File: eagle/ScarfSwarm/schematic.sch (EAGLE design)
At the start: 8 parts, among them IC1 WS2811-SOP8, M1 WIRELESS-NRF24L01

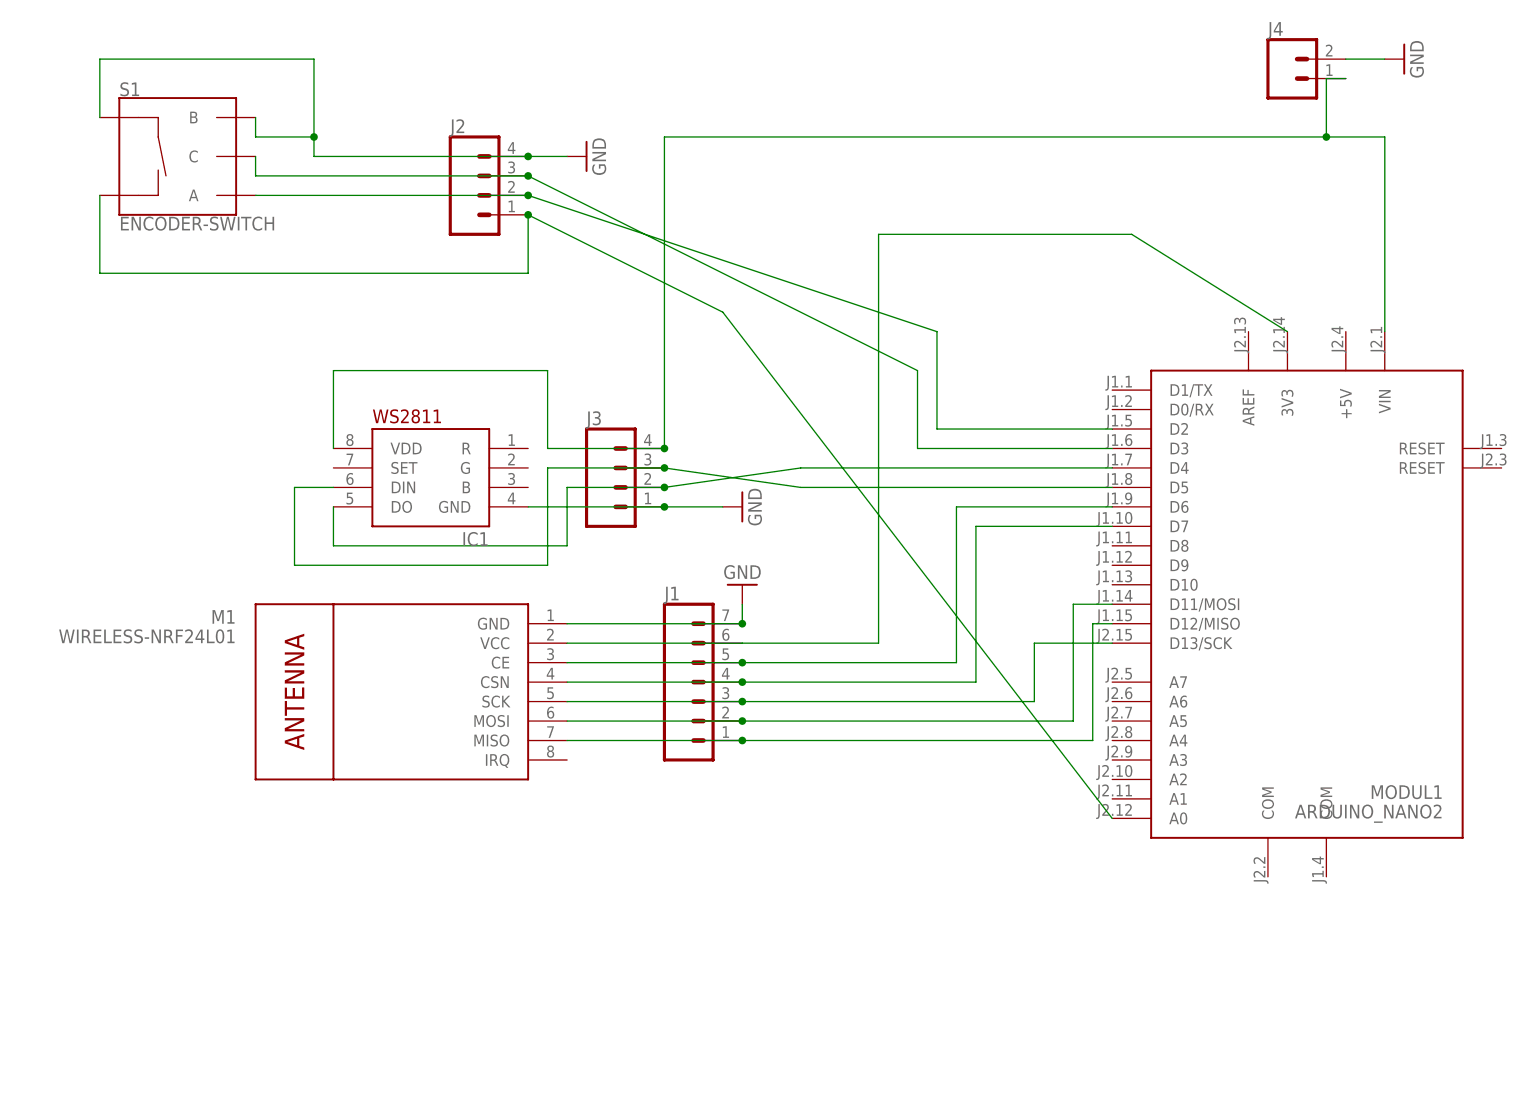
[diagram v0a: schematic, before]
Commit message: try trimming off th external componetns, first board layout
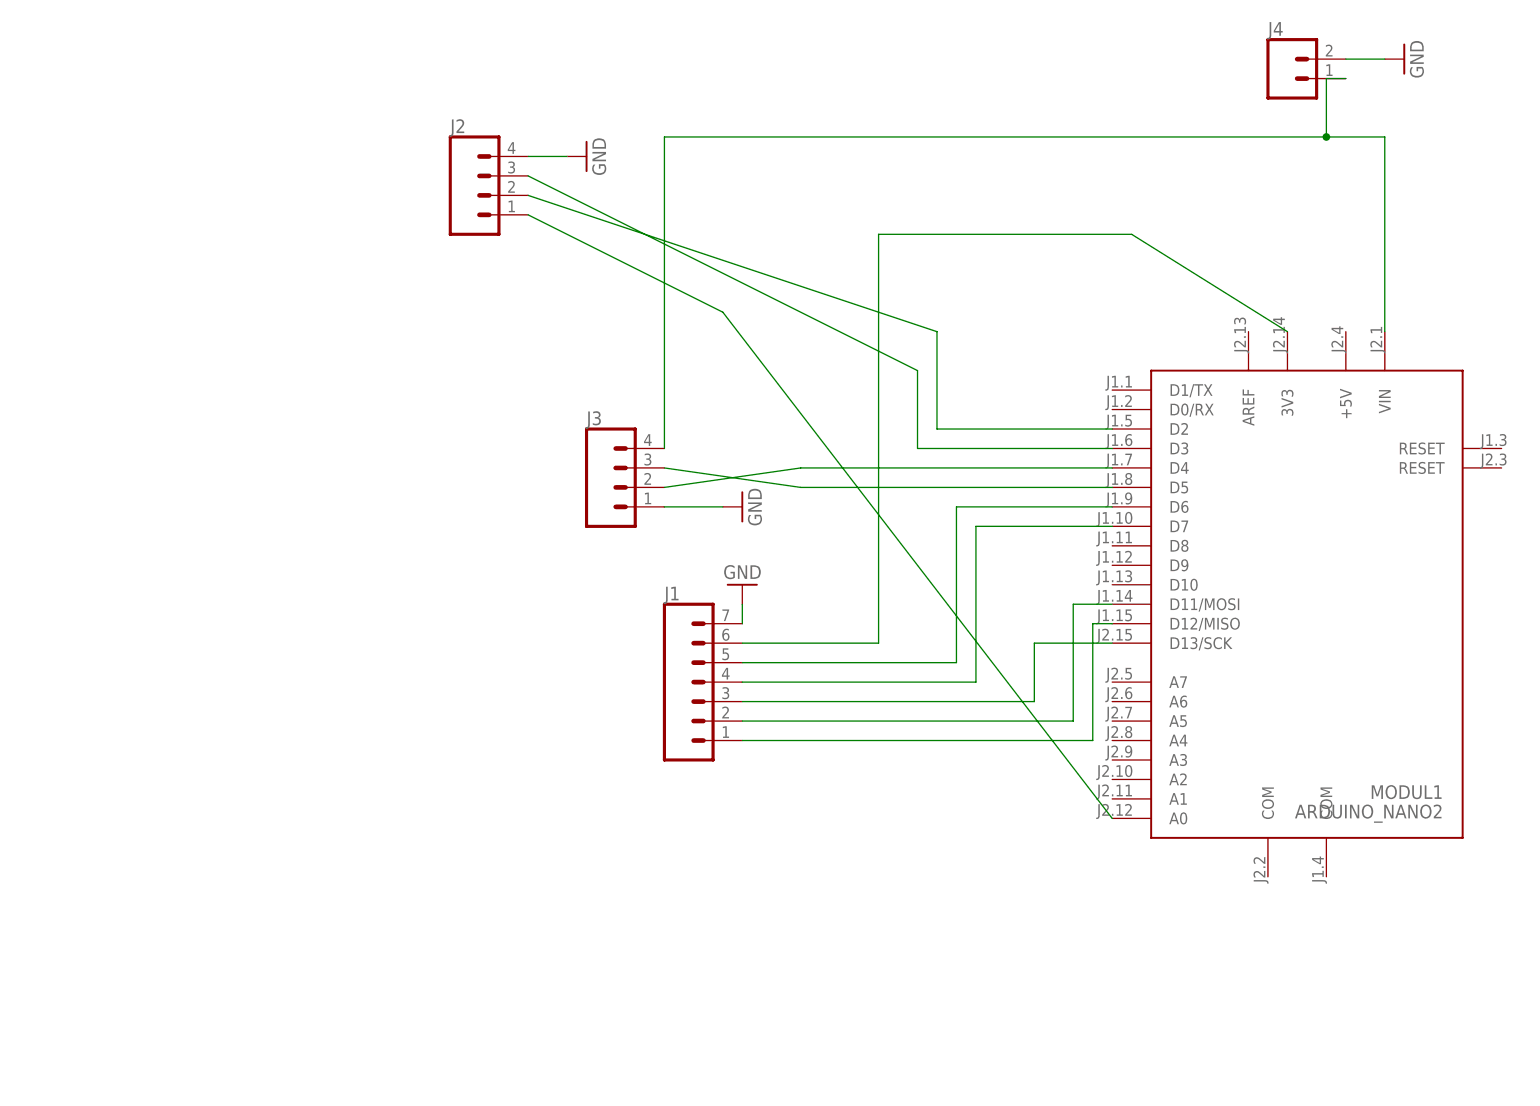
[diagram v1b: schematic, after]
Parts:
- removed IC1: WS2811-SOP8, adafruit:WS2811-SOP8
- removed M1: WIRELESS-NRF24L01, diy-modules (1):WIRELESS-NRF24L01
- removed S1: ENCODER-SWITCH, SparkFun-Switches:ENCODER-SWITCH
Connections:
- removed net N$7: IC1.DIN, J3.3, MODUL1.D5
- new net N$13: J3.3, MODUL1.D5
- net GND: no longer IC1.GND, M1.GND, S1.B, S1.SW+
- net N$1: no longer M1.VCC
- net N$10: no longer S1.A
- net N$11: no longer S1.SW-
- net N$12: no longer IC1.VDD
- net N$2: no longer M1.CE
- net N$3: no longer M1.CSN
- net N$4: no longer M1.SCK
- net N$5: no longer M1.MOSI
- net N$6: no longer M1.MISO
- net N$8: no longer IC1.DO
- net N$9: no longer S1.C
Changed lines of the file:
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@@
 <parts>
 <part name="MODUL1" library="arduino" deviceset="ARDUINO_NANO2" device=""/>
-<part name="S1" library="SparkFun-Switches" deviceset="ENCODER-SWITCH" device=""/>
 <part name="GND1" library="supply1" library_urn="urn:adsk.eagle:library:371" deviceset="GND" device=""/>
-<part name="IC1" library="adafruit" deviceset="WS2811" device="-SOP8"/>
-<part name="M1" library="diy-modules (1)" deviceset="WIRELESS-NRF24L01" device=""/>
 <part name="GND3" library="supply1" library_urn="urn:adsk.eagle:library:371" deviceset="GND" device=""/>
 <part name="GND4" library="supply1" library_urn="urn:adsk.eagle:library:371" deviceset="GND" device=""/>
@@
 <attribute name="VALUE" x="132.08" y="0" size="1.778" layer="96" rot="MR0"/>
 </instance>
-<instance part="S1" gate="G$1" x="-33.02" y="86.36" smashed="yes">
-<attribute name="NAME" x="-40.64" y="94.234" size="1.778" layer="95" font="vector"/>
-<attribute name="VALUE" x="-40.64" y="78.486" size="1.778" layer="96" font="vector" align="top-left"/>
-</instance>
 <instance part="GND1" gate="1" x="20.32" y="86.36" smashed="yes" rot="R90">
 <attribute name="VALUE" x="22.86" y="83.82" size="1.778" layer="96" rot="R90"/>
-</instance>
-<instance part="IC1" gate="G$1" x="0" y="43.18" smashed="yes" rot="MR0">
-<attribute name="NAME" x="7.62" y="35.56" size="1.778" layer="95" rot="MR0"/>
-</instance>
-<instance part="M1" gate="G$1" x="-5.08" y="15.24" smashed="yes" rot="MR0">
-<attribute name="NAME" x="-25.4" y="25.4" size="1.778" layer="95" rot="MR0"/>
-<attribute name="VALUE" x="-25.4" y="22.86" size="1.778" layer="96" rot="MR0"/>
 </instance>
 <instance part="GND3" gate="1" x="40.64" y="40.64" smashed="yes" rot="R90">
@@
 <pinref part="GND4" gate="1" pin="GND"/>
 <wire x1="40.64" y1="25.4" x2="40.64" y2="27.94" width="0.1524" layer="91"/>
-<pinref part="M1" gate="G$1" pin="GND"/>
-<wire x1="40.64" y1="25.4" x2="17.78" y2="25.4" width="0.1524" layer="91"/>
-<junction x="40.64" y="25.4"/>
 </segment>
 <segment>
-<pinref part="IC1" gate="G$1" pin="GND"/>
 <pinref part="J3" gate="J1" pin="1"/>
-<wire x1="12.7" y1="40.64" x2="30.48" y2="40.64" width="0.1524" layer="91"/>
 <pinref part="GND3" gate="1" pin="GND"/>
 <wire x1="30.48" y1="40.64" x2="38.1" y2="40.64" width="0.1524" layer="91"/>
-<junction x="30.48" y="40.64"/>
 </segment>
 <segment>
@@
 <pinref part="GND1" gate="1" pin="GND"/>
 <wire x1="12.7" y1="86.36" x2="17.78" y2="86.36" width="0.1524" layer="91"/>
-<pinref part="S1" gate="G$1" pin="SW+"/>
-<wire x1="-43.18" y1="91.44" x2="-43.18" y2="99.06" width="0.1524" layer="91"/>
-<wire x1="-43.18" y1="99.06" x2="-15.24" y2="99.06" width="0.1524" layer="91"/>
-<wire x1="-15.24" y1="99.06" x2="-15.24" y2="88.9" width="0.1524" layer="91"/>
-<wire x1="-15.24" y1="88.9" x2="-15.24" y2="86.36" width="0.1524" layer="91"/>
-<wire x1="-15.24" y1="86.36" x2="12.7" y2="86.36" width="0.1524" layer="91"/>
-<junction x="12.7" y="86.36"/>
-<pinref part="S1" gate="G$1" pin="B"/>
-<wire x1="-22.86" y1="91.44" x2="-22.86" y2="88.9" width="0.1524" layer="91"/>
-<wire x1="-22.86" y1="88.9" x2="-15.24" y2="88.9" width="0.1524" layer="91"/>
-<junction x="-15.24" y="88.9"/>
 </segment>
 <segment>
@@
 <segment>
 <pinref part="J1" gate="J1" pin="6"/>
-<pinref part="M1" gate="G$1" pin="VCC"/>
-<wire x1="40.64" y1="22.86" x2="17.78" y2="22.86" width="0.1524" layer="91"/>
 <wire x1="40.64" y1="22.86" x2="58.42" y2="22.86" width="0.1524" layer="91"/>
 <wire x1="58.42" y1="22.86" x2="58.42" y2="76.2" width="0.1524" layer="91"/>
@@
 <net name="N$2" class="0">
 <segment>
-<pinref part="M1" gate="G$1" pin="CE"/>
 <pinref part="J1" gate="J1" pin="5"/>
-<wire x1="17.78" y1="20.32" x2="40.64" y2="20.32" width="0.1524" layer="91"/>
 <wire x1="40.64" y1="20.32" x2="68.58" y2="20.32" width="0.1524" layer="91"/>
-<junction x="40.64" y="20.32"/>
 <wire x1="68.58" y1="20.32" x2="68.58" y2="40.64" width="0.1524" layer="91"/>
 <pinref part="MODUL1" gate="MODUL" pin="D6"/>
@@
 <net name="N$3" class="0">
 <segment>
-<pinref part="M1" gate="G$1" pin="CSN"/>
 <pinref part="J1" gate="J1" pin="4"/>
-<wire x1="17.78" y1="17.78" x2="40.64" y2="17.78" width="0.1524" layer="91"/>
 <wire x1="40.64" y1="17.78" x2="71.12" y2="17.78" width="0.1524" layer="91"/>
-<junction x="40.64" y="17.78"/>
 <wire x1="71.12" y1="17.78" x2="71.12" y2="38.1" width="0.1524" layer="91"/>
 <pinref part="MODUL1" gate="MODUL" pin="D7"/>
@@
 <net name="N$4" class="0">
 <segment>
-<pinref part="M1" gate="G$1" pin="SCK"/>
 <pinref part="J1" gate="J1" pin="3"/>
-<wire x1="17.78" y1="15.24" x2="40.64" y2="15.24" width="0.1524" layer="91"/>
 <wire x1="40.64" y1="15.24" x2="78.74" y2="15.24" width="0.1524" layer="91"/>
-<junction x="40.64" y="15.24"/>
 <wire x1="78.74" y1="15.24" x2="78.74" y2="22.86" width="0.1524" layer="91"/>
 <pinref part="MODUL1" gate="MODUL" pin="D13/SCK"/>
@@
 <net name="N$5" class="0">
 <segment>
-<pinref part="M1" gate="G$1" pin="MOSI"/>
 <pinref part="J1" gate="J1" pin="2"/>
-<wire x1="17.78" y1="12.7" x2="40.64" y2="12.7" width="0.1524" layer="91"/>
 <wire x1="40.64" y1="12.7" x2="83.82" y2="12.7" width="0.1524" layer="91"/>
-<junction x="40.64" y="12.7"/>
 <pinref part="MODUL1" gate="MODUL" pin="D11/MOSI"/>
 <wire x1="83.82" y1="12.7" x2="83.82" y2="27.94" width="0.1524" layer="91"/>
@@
 <net name="N$6" class="0">
 <segment>
-<pinref part="M1" gate="G$1" pin="MISO"/>
 <pinref part="J1" gate="J1" pin="1"/>
-<wire x1="17.78" y1="10.16" x2="40.64" y2="10.16" width="0.1524" layer="91"/>
 <pinref part="MODUL1" gate="MODUL" pin="D12/MISO"/>
 <wire x1="88.9" y1="25.4" x2="86.36" y2="25.4" width="0.1524" layer="91"/>
 <wire x1="86.36" y1="25.4" x2="86.36" y2="10.16" width="0.1524" layer="91"/>
 <wire x1="86.36" y1="10.16" x2="40.64" y2="10.16" width="0.1524" layer="91"/>
-<junction x="40.64" y="10.16"/>
-</segment>
-</net>
-<net name="N$7" class="0">
-<segment>
-<pinref part="J3" gate="J1" pin="3"/>
-<wire x1="30.48" y1="45.72" x2="48.26" y2="43.18" width="0.1524" layer="91"/>
-<wire x1="48.26" y1="43.18" x2="88.9" y2="43.18" width="0.1524" layer="91"/>
-<pinref part="MODUL1" gate="MODUL" pin="D5"/>
-<wire x1="30.48" y1="45.72" x2="15.24" y2="45.72" width="0.1524" layer="91"/>
-<wire x1="15.24" y1="45.72" x2="15.24" y2="33.02" width="0.1524" layer="91"/>
-<junction x="30.48" y="45.72"/>
-<wire x1="15.24" y1="33.02" x2="-17.78" y2="33.02" width="0.1524" layer="91"/>
-<pinref part="IC1" gate="G$1" pin="DIN"/>
-<wire x1="-17.78" y1="33.02" x2="-17.78" y2="43.18" width="0.1524" layer="91"/>
-<wire x1="-17.78" y1="43.18" x2="-12.7" y2="43.18" width="0.1524" layer="91"/>
 </segment>
 </net>
@@
 <wire x1="30.48" y1="43.18" x2="48.26" y2="45.72" width="0.1524" layer="91"/>
 <wire x1="48.26" y1="45.72" x2="88.9" y2="45.72" width="0.1524" layer="91"/>
-<wire x1="30.48" y1="43.18" x2="17.78" y2="43.18" width="0.1524" layer="91"/>
-<junction x="30.48" y="43.18"/>
-<wire x1="17.78" y1="43.18" x2="17.78" y2="35.56" width="0.1524" layer="91"/>
-<wire x1="17.78" y1="35.56" x2="-12.7" y2="35.56" width="0.1524" layer="91"/>
-<pinref part="IC1" gate="G$1" pin="DO"/>
-<wire x1="-12.7" y1="35.56" x2="-12.7" y2="40.64" width="0.1524" layer="91"/>
 </segment>
 </net>
@@
 <pinref part="MODUL1" gate="MODUL" pin="D3"/>
 <wire x1="63.5" y1="48.26" x2="88.9" y2="48.26" width="0.1524" layer="91"/>
-<pinref part="S1" gate="G$1" pin="C"/>
-<wire x1="-22.86" y1="86.36" x2="-22.86" y2="83.82" width="0.1524" layer="91"/>
-<wire x1="-22.86" y1="83.82" x2="12.7" y2="83.82" width="0.1524" layer="91"/>
-<junction x="12.7" y="83.82"/>
 </segment>
 </net>
@@
 <pinref part="MODUL1" gate="MODUL" pin="D2"/>
 <wire x1="66.04" y1="50.8" x2="88.9" y2="50.8" width="0.1524" layer="91"/>
-<pinref part="S1" gate="G$1" pin="A"/>
-<wire x1="-22.86" y1="81.28" x2="12.7" y2="81.28" width="0.1524" layer="91"/>
-<junction x="12.7" y="81.28"/>
 </segment>
 </net>
@@
 <pinref part="MODUL1" gate="MODUL" pin="A0"/>
 <wire x1="38.1" y1="66.04" x2="88.9" y2="0" width="0.1524" layer="91"/>
-<wire x1="12.7" y1="78.74" x2="12.7" y2="71.12" width="0.1524" layer="91"/>
-<wire x1="12.7" y1="71.12" x2="-43.18" y2="71.12" width="0.1524" layer="91"/>
-<junction x="12.7" y="78.74"/>
-<pinref part="S1" gate="G$1" pin="SW-"/>
-<wire x1="-43.18" y1="71.12" x2="-43.18" y2="81.28" width="0.1524" layer="91"/>
 </segment>
 </net>
@@
 <wire x1="116.84" y1="88.9" x2="124.46" y2="88.9" width="0.1524" layer="91"/>
 <wire x1="124.46" y1="88.9" x2="124.46" y2="63.5" width="0.1524" layer="91"/>
-<wire x1="30.48" y1="48.26" x2="15.24" y2="48.26" width="0.1524" layer="91"/>
-<wire x1="15.24" y1="48.26" x2="15.24" y2="58.42" width="0.1524" layer="91"/>
-<junction x="30.48" y="48.26"/>
-<pinref part="IC1" gate="G$1" pin="VDD"/>
-<wire x1="15.24" y1="58.42" x2="-12.7" y2="58.42" width="0.1524" layer="91"/>
-<wire x1="-12.7" y1="58.42" x2="-12.7" y2="48.26" width="0.1524" layer="91"/>
 </segment>
 </net>
+<net name="N$13" class="0">
+<segment>
+<pinref part="MODUL1" gate="MODUL" pin="D5"/>
+<wire x1="48.26" y1="43.18" x2="88.9" y2="43.18" width="0.1524" layer="91"/>
+<pinref part="J3" gate="J1" pin="3"/>
+<wire x1="30.48" y1="45.72" x2="48.26" y2="43.18" width="0.1524" layer="91"/>
+</segment>
+</net>

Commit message: swapped out arduino lib, still have errors
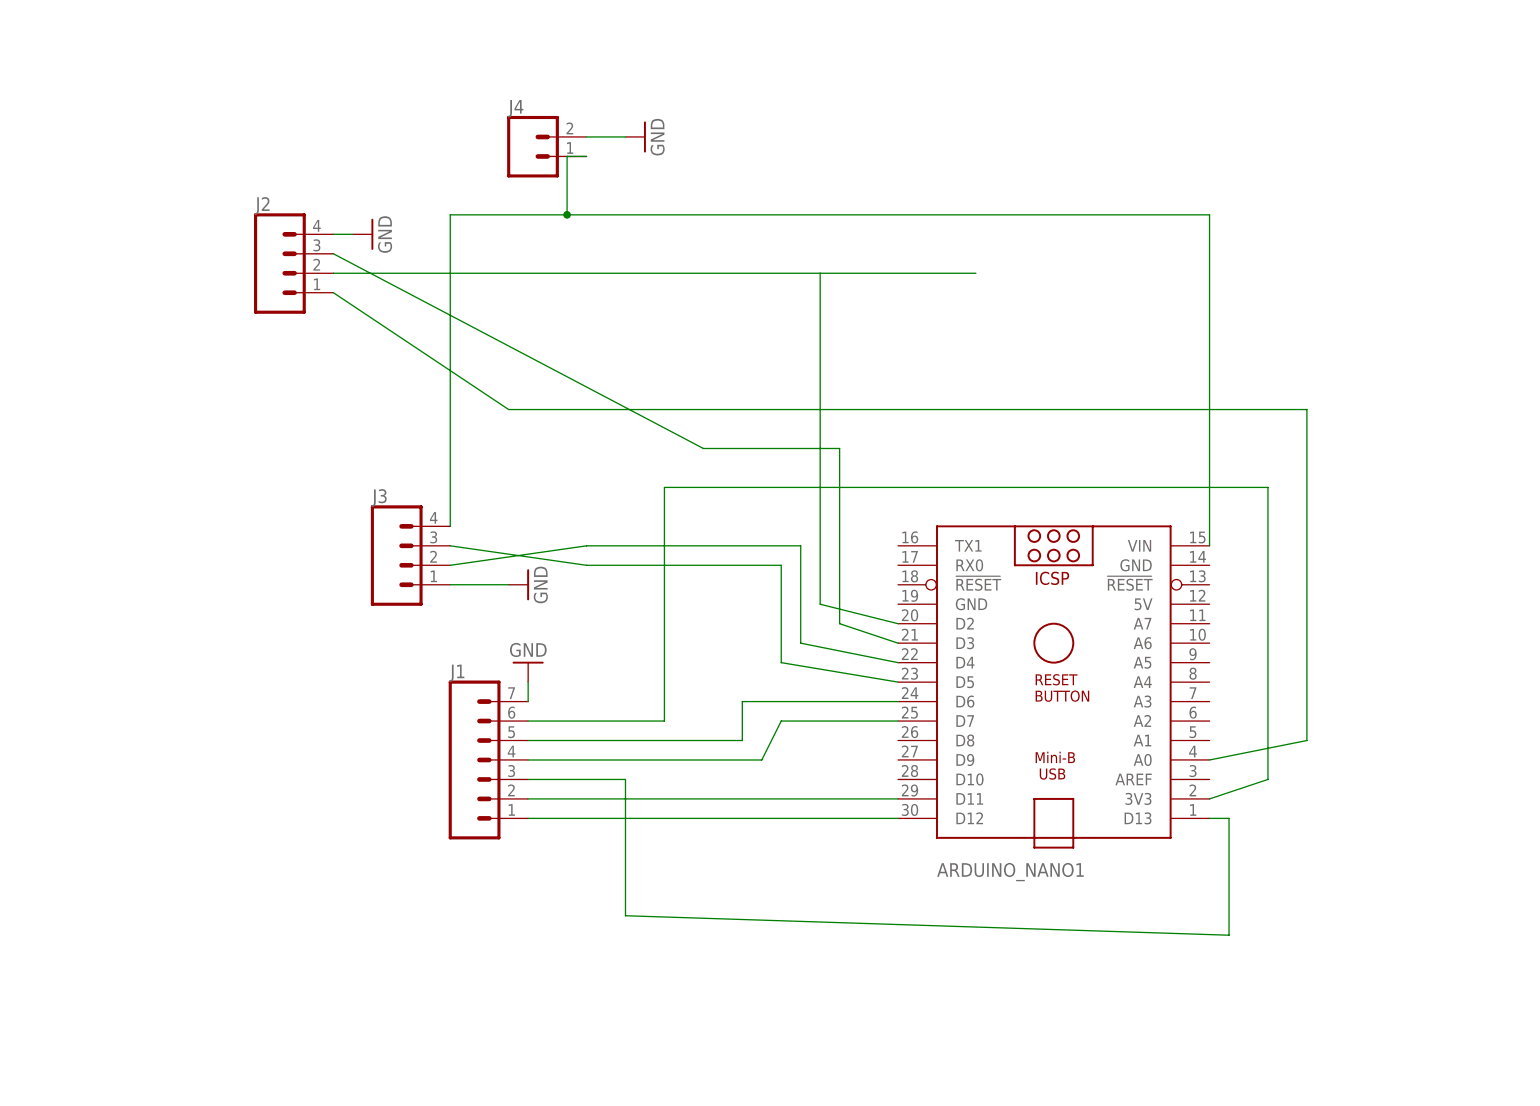
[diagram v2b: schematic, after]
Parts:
- removed MODUL1: ARDUINO_NANO2, arduino:ARDUINO_NANO2
- added ARDUINO_NANO1: (no value), ArduinoNanoV30:ARDUINO_NANO
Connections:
- net N$1: now also ARDUINO_NANO1.3V3; no longer MODUL1.3V3
- net N$10: now also ARDUINO_NANO1.D2; no longer MODUL1.D2
- net N$11: now also ARDUINO_NANO1.A0; no longer MODUL1.A0
- net N$12: now also ARDUINO_NANO1.VIN; no longer MODUL1.VIN
- net N$13: now also ARDUINO_NANO1.D5; no longer MODUL1.D5
- net N$2: now also ARDUINO_NANO1.D6; no longer MODUL1.D6
- net N$3: now also ARDUINO_NANO1.D7; no longer MODUL1.D7
- net N$4: now also ARDUINO_NANO1.D13; no longer MODUL1.D13/SCK
- net N$5: now also ARDUINO_NANO1.D11; no longer MODUL1.D11/MOSI
- net N$6: now also ARDUINO_NANO1.D12; no longer MODUL1.D12/MISO
- net N$8: now also ARDUINO_NANO1.D4; no longer MODUL1.D4
- net N$9: now also ARDUINO_NANO1.D3; no longer MODUL1.D3
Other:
- moved on the sheet: J1, J2, J3, J4
